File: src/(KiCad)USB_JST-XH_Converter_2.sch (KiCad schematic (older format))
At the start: 12 parts, among them U1 TCKE805NAWSON10B_TOS-REC

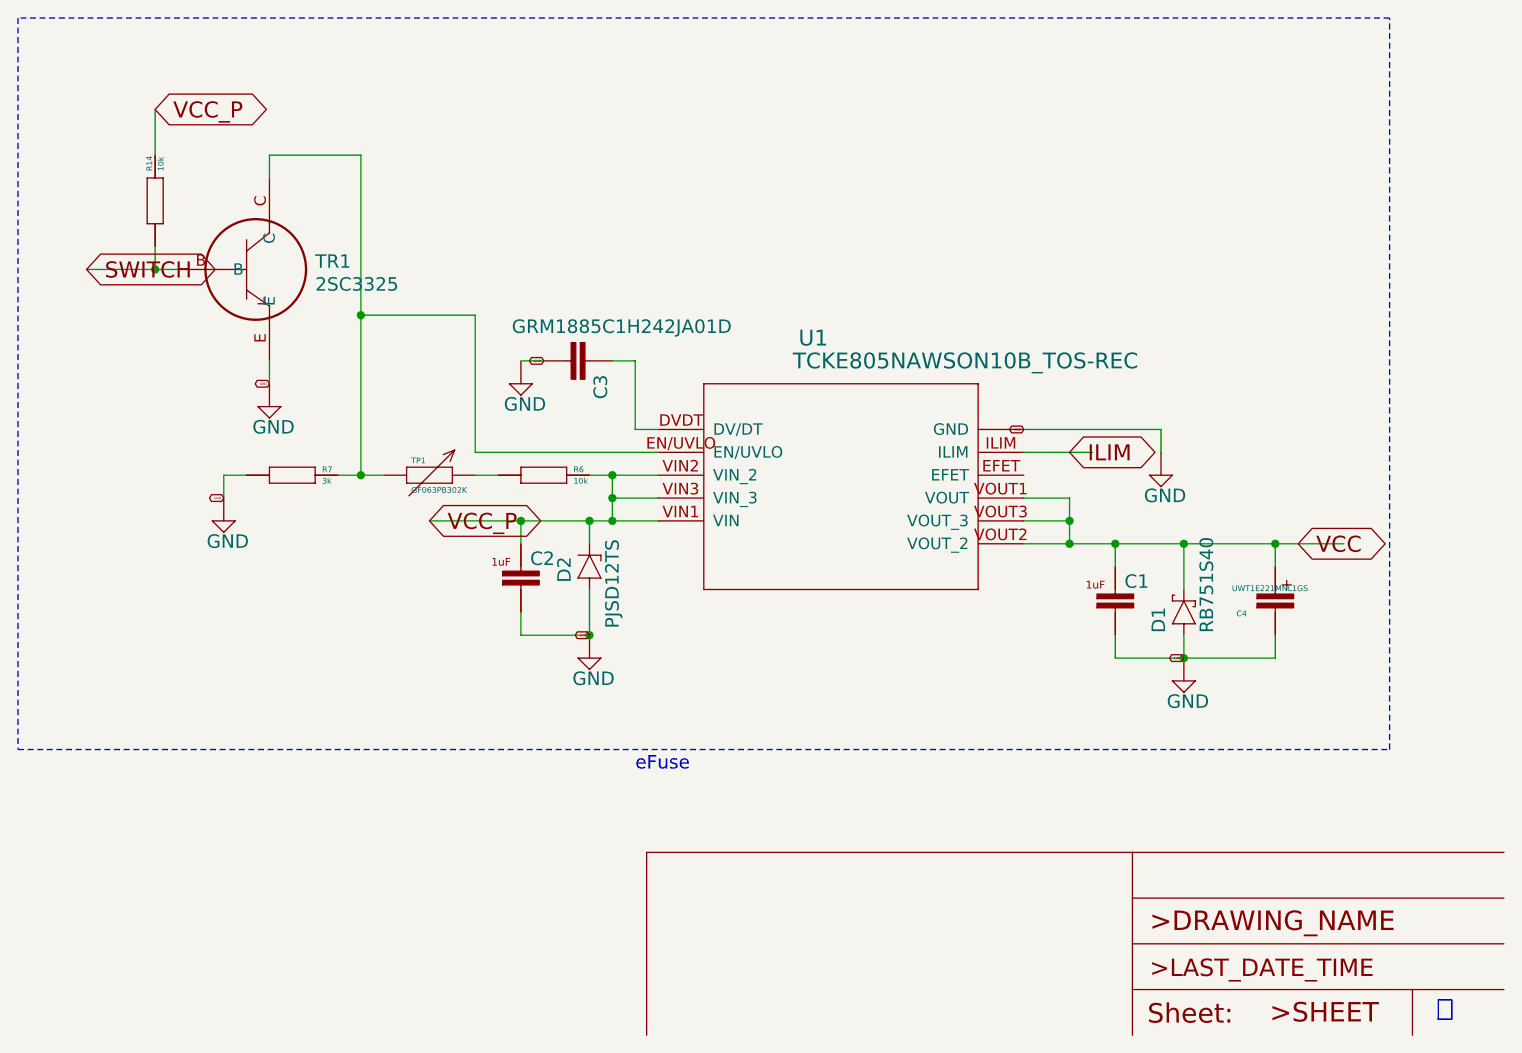
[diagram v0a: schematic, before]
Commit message: 3Aモード用LEDの追加
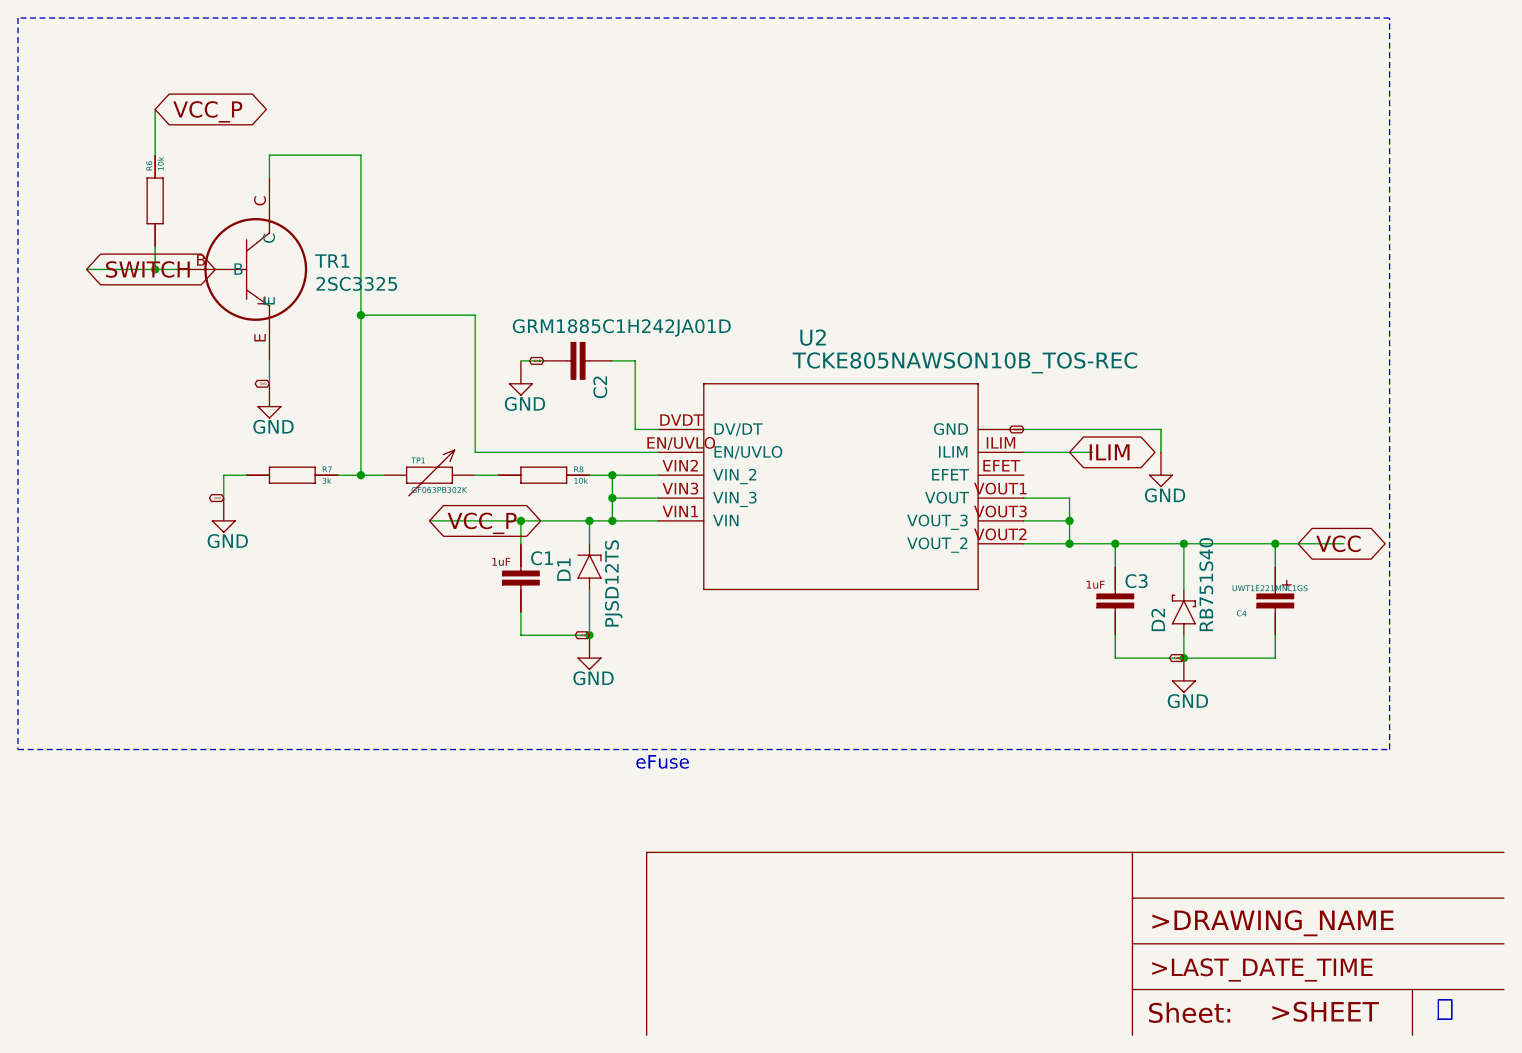
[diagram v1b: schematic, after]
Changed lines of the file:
@@
 AR Path="/B9163575" Ref="#FRAME2"  Part="1"
 AR Path="/639B4D5D/B9163575" Ref="#FRAME2"  Part="1"
+AR Path="/639EC9D1/B9163575" Ref="#FRAME2"  Part="1"
 F 0 "#FRAME2" H 2300 6400 50  0001 C CNN
 F 1 "A5L-LOC" H 2300 6400 50  0001 C CNN
@@
 AR Path="/20B1DDDE" Ref="#SUPPLY5"  Part="1"
 AR Path="/639B4D5D/20B1DDDE" Ref="#SUPPLY05"  Part="1"
-F 0 "#SUPPLY05" H 7900 3800 50  0001 C CNN
+AR Path="/639EC9D1/20B1DDDE" Ref="#SUPPLY0105"  Part="1"
+F 0 "#SUPPLY0105" H 7900 3800 50  0001 C CNN
 F 1 "GND" H 7825 3675 59  0000 L BNN
 F 2 "" H 7900 3800 50  0001 C CNN
@@
 AR Path="/24F56349" Ref="C1"  Part="1"
 AR Path="/639B4D5D/24F56349" Ref="C1"  Part="1"
-F 0 "C1" H 7740 4300 59  0000 L BNN
+AR Path="/639EC9D1/24F56349" Ref="C3"  Part="1"
+F 0 "C3" H 7740 4300 59  0000 L BNN
 F 1 "GRM21BC72A105KE01" H 7700 4300 50  0001 C CNN
 F 2 "USB_JST-XH_Converter:GRM21BC72A105KE01" H 7700 4300 50  0001 C CNN
@@
 AR Path="/A7CD5EB6" Ref="#SUPPLY6"  Part="1"
 AR Path="/639B4D5D/A7CD5EB6" Ref="#SUPPLY06"  Part="1"
-F 0 "#SUPPLY06" H 8000 4700 50  0001 C CNN
+AR Path="/639EC9D1/A7CD5EB6" Ref="#SUPPLY0106"  Part="1"
+F 0 "#SUPPLY0106" H 8000 4700 50  0001 C CNN
 F 1 "GND" H 7925 4575 59  0000 L BNN
 F 2 "" H 8000 4700 50  0001 C CNN
@@
 AR Path="/4071D1F9" Ref="C2"  Part="1"
 AR Path="/639B4D5D/4071D1F9" Ref="C2"  Part="1"
-F 0 "C2" H 5140 4200 59  0000 L BNN
+AR Path="/639EC9D1/4071D1F9" Ref="C1"  Part="1"
+F 0 "C1" H 5140 4200 59  0000 L BNN
 F 1 "GRM21BC72A105KE01" H 5100 4200 50  0001 C CNN
 F 2 "USB_JST-XH_Converter:GRM21BC72A105KE01" H 5100 4200 50  0001 C CNN
@@
 AR Path="/2907E397" Ref="#SUPPLY7"  Part="1"
 AR Path="/639B4D5D/2907E397" Ref="#SUPPLY07"  Part="1"
-F 0 "#SUPPLY07" H 5400 4600 50  0001 C CNN
+AR Path="/639EC9D1/2907E397" Ref="#SUPPLY0107"  Part="1"
+F 0 "#SUPPLY0107" H 5400 4600 50  0001 C CNN
 F 1 "GND" H 5325 4475 59  0000 L BNN
 F 2 "" H 5400 4600 50  0001 C CNN
@@
 AR Path="/39566F8A" Ref="#SUPPLY8"  Part="1"
 AR Path="/639B4D5D/39566F8A" Ref="#SUPPLY08"  Part="1"
-F 0 "#SUPPLY08" H 5100 3400 50  0001 C CNN
+AR Path="/639EC9D1/39566F8A" Ref="#SUPPLY0108"  Part="1"
+F 0 "#SUPPLY0108" H 5100 3400 50  0001 C CNN
 F 1 "GND" H 5025 3275 59  0000 L BNN
 F 2 "" H 5100 3400 50  0001 C CNN
@@
 AR Path="/1047F363" Ref="R6"  Part="1"
 AR Path="/639B4D5D/1047F363" Ref="R6"  Part="1"
-F 0 "R6" H 5330 3810 25  0000 L BNN
+AR Path="/639EC9D1/1047F363" Ref="R8"  Part="1"
+F 0 "R8" H 5330 3810 25  0000 L BNN
 F 1 "10k" H 5330 3760 25  0000 L BNN
 F 2 "USB_JST-XH_Converter:RG2012" H 5200 3800 50  0001 C CNN
@@
 AR Path="/8EDB071B" Ref="R7"  Part="1"
 AR Path="/639B4D5D/8EDB071B" Ref="R7"  Part="1"
+AR Path="/639EC9D1/8EDB071B" Ref="R7"  Part="1"
 F 0 "R7" H 4230 3810 25  0000 L BNN
 F 1 "3k" H 4230 3760 25  0000 L BNN
@@
 AR Path="/B8640D54" Ref="#SUPPLY9"  Part="1"
 AR Path="/639B4D5D/B8640D54" Ref="#SUPPLY09"  Part="1"
-F 0 "#SUPPLY09" H 3800 4000 50  0001 C CNN
+AR Path="/639EC9D1/B8640D54" Ref="#SUPPLY0109"  Part="1"
+F 0 "#SUPPLY0109" H 3800 4000 50  0001 C CNN
 F 1 "GND" H 3725 3875 59  0000 L BNN
 F 2 "" H 3800 4000 50  0001 C CNN
@@
 AR Path="/FE5B29FD" Ref="TP1"  Part="1"
 AR Path="/639B4D5D/FE5B29FD" Ref="TP1"  Part="1"
+AR Path="/639EC9D1/FE5B29FD" Ref="TP1"  Part="1"
 F 0 "TP1" H 4620 3849 25  0000 L BNN
 F 1 "GF063PB302K" H 4620 3720 25  0000 L BNN
@@
 AR Path="/8D803956" Ref="#SUPPLY13"  Part="1"
 AR Path="/639B4D5D/8D803956" Ref="#SUPPLY013"  Part="1"
-F 0 "#SUPPLY013" H 4000 3500 50  0001 C CNN
+AR Path="/639EC9D1/8D803956" Ref="#SUPPLY0110"  Part="1"
+F 0 "#SUPPLY0110" H 4000 3500 50  0001 C CNN
 F 1 "GND" H 3925 3375 59  0000 L BNN
 F 2 "" H 4000 3500 50  0001 C CNN
@@
 AR Path="/5915D5B8" Ref="R14"  Part="1"
 AR Path="/639B4D5D/5915D5B8" Ref="R14"  Part="1"
-F 0 "R14" H 3630 2610 25  0000 L BNN
+AR Path="/639EC9D1/5915D5B8" Ref="R6"  Part="1"
+F 0 "R6" H 3630 2610 25  0000 L BNN
 F 1 "10k" H 3630 2560 25  0000 L BNN
 F 2 "USB_JST-XH_Converter:RG2012" H 3500 2600 50  0001 C CNN
@@
 AR Path="/A9286F55" Ref="TR1"  Part="1"
 AR Path="/639B4D5D/A9286F55" Ref="TR1"  Part="1"
+AR Path="/639EC9D1/A9286F55" Ref="TR1"  Part="1"
 F 0 "TR1" H 4200 2900 59  0000 L BNN
 F 1 "2SC3325" H 4200 2800 59  0000 L BNN
@@
 AR Path="/0CADE672" Ref="D2"  Part="1"
 AR Path="/639B4D5D/0CADE672" Ref="D2"  Part="1"
-F 0 "D2" H 5330 4275 59  0000 L BNN
+AR Path="/639EC9D1/0CADE672" Ref="D1"  Part="1"
+F 0 "D1" H 5330 4275 59  0000 L BNN
 F 1 "PJSD12TS" H 5130 4065 59  0000 L BNN
 F 2 "USB_JST-XH_Converter:SOD-523" H 5400 4200 50  0001 C CNN
@@
 AR Path="/C78C3FBD" Ref="D1"  Part="1"
 AR Path="/639B4D5D/C78C3FBD" Ref="D1"  Part="1"
-F 0 "D1" H 7910 4475 59  0000 L BNN
+AR Path="/639EC9D1/C78C3FBD" Ref="D2"  Part="1"
+F 0 "D2" H 7910 4475 59  0000 L BNN
 F 1 "RB751S40" H 7910 4265 59  0000 L BNN
 F 2 "USB_JST-XH_Converter:SOD-523" H 8000 4400 50  0001 C CNN
@@
 AR Path="/00CB58E1" Ref="C3"  Part="1"
 AR Path="/639B4D5D/00CB58E1" Ref="C3"  Part="1"
-F 0 "C3" H 5460 3315 59  0000 L BNN
+AR Path="/639EC9D1/00CB58E1" Ref="C2"  Part="1"
+F 0 "C2" H 5460 3315 59  0000 L BNN
 F 1 "GRM1885C1H242JA01D" V 5285 2960 59  0000 L BNN
 F 2 "USB_JST-XH_Converter:GRM18" H 5400 3300 50  0001 C CNN
@@
 AR Path="/8B5AD75A" Ref="C4"  Part="1"
 AR Path="/639B4D5D/8B5AD75A" Ref="C4"  Part="1"
+AR Path="/639EC9D1/8B5AD75A" Ref="C4"  Part="1"
 F 0 "C4" H 8230 4180 25  0000 L BNN
 F 1 "UWT1E221MNL1GS" H 8210 4290 25  0000 L BNN
@@
 AR Path="/94FABF20" Ref="U1"  Part="1"
 AR Path="/639B4D5D/94FABF20" Ref="U1"  Part="1"
-F 0 "U1" H 6314 3959 69  0000 L BNN
+AR Path="/639EC9D1/94FABF20" Ref="U2"  Part="1"
+F 0 "U2" H 6314 3959 69  0000 L BNN
 F 1 "TCKE805NAWSON10B_TOS-REC" H 6289 3859 69  0000 L BNN
 F 2 "USB_JST-XH_Converter:WSON10B_TOS-RIC" H 5600 3600 50  0001 C CNN

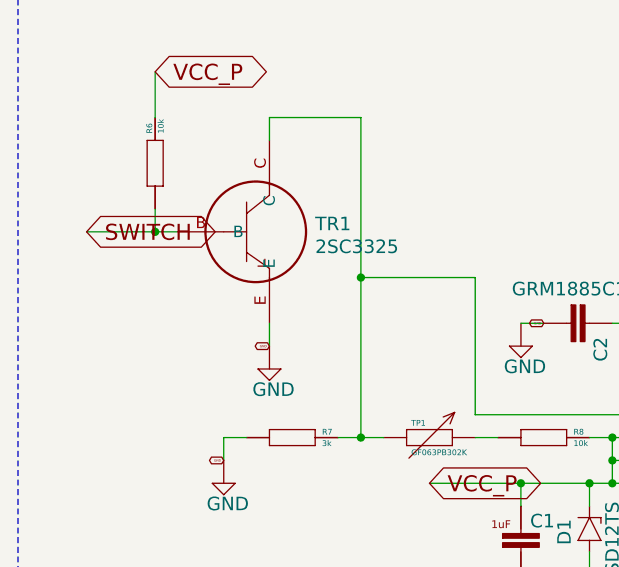
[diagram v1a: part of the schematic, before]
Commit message: 微修正、BJTのBS間抵抗の追加
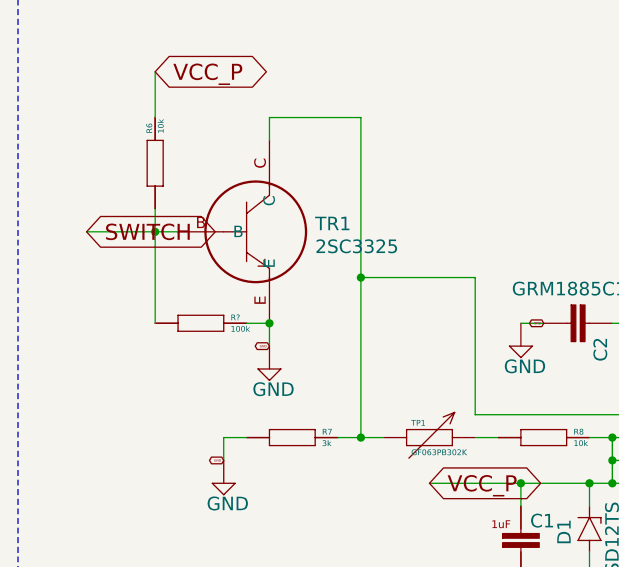
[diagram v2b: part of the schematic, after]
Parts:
- added R?: 100k, USB_JST-XH_Converter:RG2012, symbol USB_JST-XH_Converter-eagle-import:RG2012
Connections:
- wire segments 55 -> 57
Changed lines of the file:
@@
 $Descr A4 11693 8268
 encoding utf-8
-Sheet 1 4
+Sheet 3 4
 Title ""
 Date ""
@@
 Text Notes 9100 6200 0    85   ~ 0
 完
+$Comp
+L USB_JST-XH_Converter-eagle-import:RG2012 R?
+U 1 1 63A2BE04
+P 3700 3300
+AR Path="/63A2BE04" Ref="R?"  Part="1"
+AR Path="/639B4D5D/63A2BE04" Ref="R?"  Part="1"
+AR Path="/639EC9D1/63A2BE04" Ref="R?"  Part="1"
+F 0 "R?" H 3830 3310 25  0000 L BNN
+F 1 "100k" H 3830 3260 25  0000 L BNN
+F 2 "USB_JST-XH_Converter:RG2012" H 3700 3300 50  0001 C CNN
+F 3 "" H 3700 3300 50  0001 C CNN
+	1    3700 3300
+	1    0    0    -1
+$EndComp
+Wire Wire Line
+	3900 3300 4000 3300
+Connection ~ 4000 3300
+Wire Wire Line
+	3500 3300 3500 2900
 $EndSCHEMATC
